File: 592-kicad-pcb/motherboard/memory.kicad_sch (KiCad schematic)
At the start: 13 parts, among them J15 Micro_SD_Card, J16 Conn_02x01, U12 W25Q32JVSS, U13 SN74LVC1G3157DBVR

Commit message: updates to routing
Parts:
- renumbered C29 to C31, C30 to C32, C31 to C33, C32 to C34, C33 to C35, J15 to J19, J16 to J20, R54 to R48, R55 to R49, R47 to R50, U12 to U13, U13 to U14
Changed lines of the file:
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@@
 		(dnp no)
 		(fields_autoplaced yes)
-		(property "Reference" "#PWR0141"
+		(property "Reference" "#PWR0143"
 			(at 46.99 52.07 0)
 			(effects
@@
 			(project "motherboard"
 				(path "/5b0c97ac-fa03-4db8-b41b-0eee32b6f55d/f049e4ad-bebe-4338-850a-2727de737ae9/2022d8e8-455b-4f4a-b4b4-f79e7486e2af"
-					(reference "#PWR0141")
+					(reference "#PWR0143")
 					(unit 1)
 				)
@@
 		(on_board yes)
 		(dnp no)
-		(property "Reference" "C33"
+		(property "Reference" "C35"
 			(at 201.93 81.2862 0)
 			(effects
@@
 			(project "motherboard"
 				(path "/5b0c97ac-fa03-4db8-b41b-0eee32b6f55d/f049e4ad-bebe-4338-850a-2727de737ae9/2022d8e8-455b-4f4a-b4b4-f79e7486e2af"
-					(reference "C33")
+					(reference "C35")
 					(unit 1)
 				)
@@
 		(on_board yes)
 		(dnp no)
-		(property "Reference" "C31"
+		(property "Reference" "C33"
 			(at 113.284 66.548 0)
 			(effects
@@
 			(project "motherboard"
 				(path "/5b0c97ac-fa03-4db8-b41b-0eee32b6f55d/f049e4ad-bebe-4338-850a-2727de737ae9/2022d8e8-455b-4f4a-b4b4-f79e7486e2af"
-					(reference "C31")
+					(reference "C33")
 					(unit 1)
 				)
@@
 		(on_board yes)
 		(dnp no)
-		(property "Reference" "#PWR0149"
+		(property "Reference" "#PWR0155"
 			(at 193.04 95.25 0)
 			(effects
@@
 			(project "motherboard"
 				(path "/5b0c97ac-fa03-4db8-b41b-0eee32b6f55d/f049e4ad-bebe-4338-850a-2727de737ae9/2022d8e8-455b-4f4a-b4b4-f79e7486e2af"
-					(reference "#PWR0149")
+					(reference "#PWR0155")
 					(unit 1)
 				)
@@
 		(dnp no)
 		(fields_autoplaced yes)
-		(property "Reference" "R47"
+		(property "Reference" "R50"
 			(at 195.58 62.2299 0)
 			(effects
@@
 			(project "motherboard"
 				(path "/5b0c97ac-fa03-4db8-b41b-0eee32b6f55d/f049e4ad-bebe-4338-850a-2727de737ae9/2022d8e8-455b-4f4a-b4b4-f79e7486e2af"
-					(reference "R47")
+					(reference "R50")
 					(unit 1)
 				)
@@
 		(on_board yes)
 		(dnp no)
-		(property "Reference" "C29"
+		(property "Reference" "C31"
 			(at 94.234 131.318 0)
 			(effects
@@
 			(project "motherboard"
 				(path "/5b0c97ac-fa03-4db8-b41b-0eee32b6f55d/f049e4ad-bebe-4338-850a-2727de737ae9/2022d8e8-455b-4f4a-b4b4-f79e7486e2af"
-					(reference "C29")
+					(reference "C31")
 					(unit 1)
 				)
@@
 		(dnp no)
 		(fields_autoplaced yes)
-		(property "Reference" "#PWR0144"
+		(property "Reference" "#PWR0150"
 			(at 119.38 60.96 0)
 			(effects
@@
 			(project "motherboard"
 				(path "/5b0c97ac-fa03-4db8-b41b-0eee32b6f55d/f049e4ad-bebe-4338-850a-2727de737ae9/2022d8e8-455b-4f4a-b4b4-f79e7486e2af"
-					(reference "#PWR0144")
+					(reference "#PWR0150")
 					(unit 1)
 				)
@@
 		(on_board yes)
 		(dnp no)
-		(property "Reference" "#PWR0140"
+		(property "Reference" "#PWR0146"
 			(at 67.31 152.4 0)
 			(effects
@@
 			(project "motherboard"
 				(path "/5b0c97ac-fa03-4db8-b41b-0eee32b6f55d/f049e4ad-bebe-4338-850a-2727de737ae9/2022d8e8-455b-4f4a-b4b4-f79e7486e2af"
-					(reference "#PWR0140")
+					(reference "#PWR0146")
 					(unit 1)
 				)
@@
 		(on_board yes)
 		(dnp no)
-		(property "Reference" "#PWR0145"
+		(property "Reference" "#PWR0151"
 			(at 119.38 78.74 0)
 			(effects
@@
 			(project "motherboard"
 				(path "/5b0c97ac-fa03-4db8-b41b-0eee32b6f55d/f049e4ad-bebe-4338-850a-2727de737ae9/2022d8e8-455b-4f4a-b4b4-f79e7486e2af"
-					(reference "#PWR0145")
+					(reference "#PWR0151")
 					(unit 1)
 				)
@@
 		(on_board yes)
 		(dnp no)
-		(property "Reference" "U13"
+		(property "Reference" "U14"
 			(at 163.576 57.15 0)
 			(effects
@@
 			(project "motherboard"
 				(path "/5b0c97ac-fa03-4db8-b41b-0eee32b6f55d/f049e4ad-bebe-4338-850a-2727de737ae9/2022d8e8-455b-4f4a-b4b4-f79e7486e2af"
-					(reference "U13")
+					(reference "U14")
 					(unit 1)
 				)
@@
 		(dnp no)
 		(fields_autoplaced yes)
-		(property "Reference" "U12"
+		(property "Reference" "U13"
 			(at 78.74 129.5399 0)
 			(effects
@@
 			(project "motherboard"
 				(path "/5b0c97ac-fa03-4db8-b41b-0eee32b6f55d/f049e4ad-bebe-4338-850a-2727de737ae9/2022d8e8-455b-4f4a-b4b4-f79e7486e2af"
-					(reference "U12")
+					(reference "U13")
 					(unit 1)
 				)
@@
 		(dnp no)
 		(fields_autoplaced yes)
-		(property "Reference" "J15"
+		(property "Reference" "J19"
 			(at 88.265 44.45 0)
 			(effects
@@
 			(project "motherboard"
 				(path "/5b0c97ac-fa03-4db8-b41b-0eee32b6f55d/f049e4ad-bebe-4338-850a-2727de737ae9/2022d8e8-455b-4f4a-b4b4-f79e7486e2af"
-					(reference "J15")
+					(reference "J19")
 					(unit 1)
 				)
@@
 		(dnp yes)
 		(fields_autoplaced yes)
-		(property "Reference" "J16"
+		(property "Reference" "J20"
 			(at 186.69 80.01 0)
 			(effects
@@
 			(project "motherboard"
 				(path "/5b0c97ac-fa03-4db8-b41b-0eee32b6f55d/f049e4ad-bebe-4338-850a-2727de737ae9/2022d8e8-455b-4f4a-b4b4-f79e7486e2af"
-					(reference "J16")
+					(reference "J20")
 					(unit 1)
 				)
@@
 		(on_board yes)
 		(dnp no)
-		(property "Reference" "C30"
+		(property "Reference" "C32"
 			(at 103.124 131.318 0)
 			(effects
@@
 			(project "motherboard"
 				(path "/5b0c97ac-fa03-4db8-b41b-0eee32b6f55d/f049e4ad-bebe-4338-850a-2727de737ae9/2022d8e8-455b-4f4a-b4b4-f79e7486e2af"
-					(reference "C30")
+					(reference "C32")
 					(unit 1)
 				)
@@
 		(on_board yes)
 		(dnp no)
-		(property "Reference" "#PWR0138"
+		(property "Reference" "#PWR0144"
 			(at 46.99 77.47 0)
 			(effects
@@
 			(project "motherboard"
 				(path "/5b0c97ac-fa03-4db8-b41b-0eee32b6f55d/f049e4ad-bebe-4338-850a-2727de737ae9/2022d8e8-455b-4f4a-b4b4-f79e7486e2af"
-					(reference "#PWR0138")
+					(reference "#PWR0144")
 					(unit 1)
 				)
@@
 		(on_board yes)
 		(dnp no)
-		(property "Reference" "R55"
+		(property "Reference" "R49"
 			(at 58.42 52.0699 0)
 			(effects
@@
 			(project "motherboard"
 				(path "/5b0c97ac-fa03-4db8-b41b-0eee32b6f55d/f049e4ad-bebe-4338-850a-2727de737ae9/2022d8e8-455b-4f4a-b4b4-f79e7486e2af"
-					(reference "R55")
+					(reference "R49")
 					(unit 1)
 				)
@@
 		(on_board yes)
 		(dnp no)
-		(property "Reference" "C32"
+		(property "Reference" "C34"
 			(at 122.174 66.548 0)
 			(effects
@@
 			(project "motherboard"
 				(path "/5b0c97ac-fa03-4db8-b41b-0eee32b6f55d/f049e4ad-bebe-4338-850a-2727de737ae9/2022d8e8-455b-4f4a-b4b4-f79e7486e2af"
-					(reference "C32")
+					(reference "C34")
 					(unit 1)
 				)
@@
 		(dnp no)
 		(fields_autoplaced yes)
-		(property "Reference" "#PWR0137"
+		(property "Reference" "#PWR0145"
 			(at 67.31 116.84 0)
 			(effects
@@
 			(project ""
 				(path "/5b0c97ac-fa03-4db8-b41b-0eee32b6f55d/f049e4ad-bebe-4338-850a-2727de737ae9/2022d8e8-455b-4f4a-b4b4-f79e7486e2af"
-					(reference "#PWR0137")
+					(reference "#PWR0145")
 					(unit 1)
 				)
@@
 		(dnp no)
 		(fields_autoplaced yes)
-		(property "Reference" "#PWR0139"
+		(property "Reference" "#PWR0147"
 			(at 100.33 125.73 0)
 			(effects
@@
 			(project "motherboard"
 				(path "/5b0c97ac-fa03-4db8-b41b-0eee32b6f55d/f049e4ad-bebe-4338-850a-2727de737ae9/2022d8e8-455b-4f4a-b4b4-f79e7486e2af"
-					(reference "#PWR0139")
+					(reference "#PWR0147")
 					(unit 1)
 				)
@@
 		(on_board yes)
 		(dnp no)
-		(property "Reference" "R54"
+		(property "Reference" "R48"
 			(at 53.34 116.8399 0)
 			(effects
@@
 			(project "motherboard"
 				(path "/5b0c97ac-fa03-4db8-b41b-0eee32b6f55d/f049e4ad-bebe-4338-850a-2727de737ae9/2022d8e8-455b-4f4a-b4b4-f79e7486e2af"
-					(reference "R54")
+					(reference "R48")
 					(unit 1)
 				)
@@
 		(dnp no)
 		(fields_autoplaced yes)
-		(property "Reference" "#PWR0148"
+		(property "Reference" "#PWR0154"
 			(at 193.04 60.96 0)
 			(effects
@@
 			(project "motherboard"
 				(path "/5b0c97ac-fa03-4db8-b41b-0eee32b6f55d/f049e4ad-bebe-4338-850a-2727de737ae9/2022d8e8-455b-4f4a-b4b4-f79e7486e2af"
-					(reference "#PWR0148")
+					(reference "#PWR0154")
 					(unit 1)
 				)
@@
 		(dnp no)
 		(fields_autoplaced yes)
-		(property "Reference" "#PWR0146"
+		(property "Reference" "#PWR0152"
 			(at 172.72 55.88 0)
 			(effects
@@
 			(project "motherboard"
 				(path "/5b0c97ac-fa03-4db8-b41b-0eee32b6f55d/f049e4ad-bebe-4338-850a-2727de737ae9/2022d8e8-455b-4f4a-b4b4-f79e7486e2af"
-					(reference "#PWR0146")
+					(reference "#PWR0152")
 					(unit 1)
 				)
@@
 		(on_board yes)
 		(dnp no)
-		(property "Reference" "#PWR0143"
+		(property "Reference" "#PWR0149"
 			(at 111.76 95.25 0)
 			(effects
@@
 			(project "motherboard"
 				(path "/5b0c97ac-fa03-4db8-b41b-0eee32b6f55d/f049e4ad-bebe-4338-850a-2727de737ae9/2022d8e8-455b-4f4a-b4b4-f79e7486e2af"
-					(reference "#PWR0143")
+					(reference "#PWR0149")
 					(unit 1)
 				)
@@
 		(on_board yes)
 		(dnp no)
-		(property "Reference" "#PWR0147"
+		(property "Reference" "#PWR0153"
 			(at 172.72 86.36 0)
 			(effects
@@
 			(project "motherboard"
 				(path "/5b0c97ac-fa03-4db8-b41b-0eee32b6f55d/f049e4ad-bebe-4338-850a-2727de737ae9/2022d8e8-455b-4f4a-b4b4-f79e7486e2af"
-					(reference "#PWR0147")
+					(reference "#PWR0153")
 					(unit 1)
 				)
@@
 		(on_board yes)
 		(dnp no)
-		(property "Reference" "#PWR0142"
+		(property "Reference" "#PWR0148"
 			(at 100.33 143.51 0)
 			(effects
@@
 			(project "motherboard"
 				(path "/5b0c97ac-fa03-4db8-b41b-0eee32b6f55d/f049e4ad-bebe-4338-850a-2727de737ae9/2022d8e8-455b-4f4a-b4b4-f79e7486e2af"
-					(reference "#PWR0142")
+					(reference "#PWR0148")
 					(unit 1)
 				)

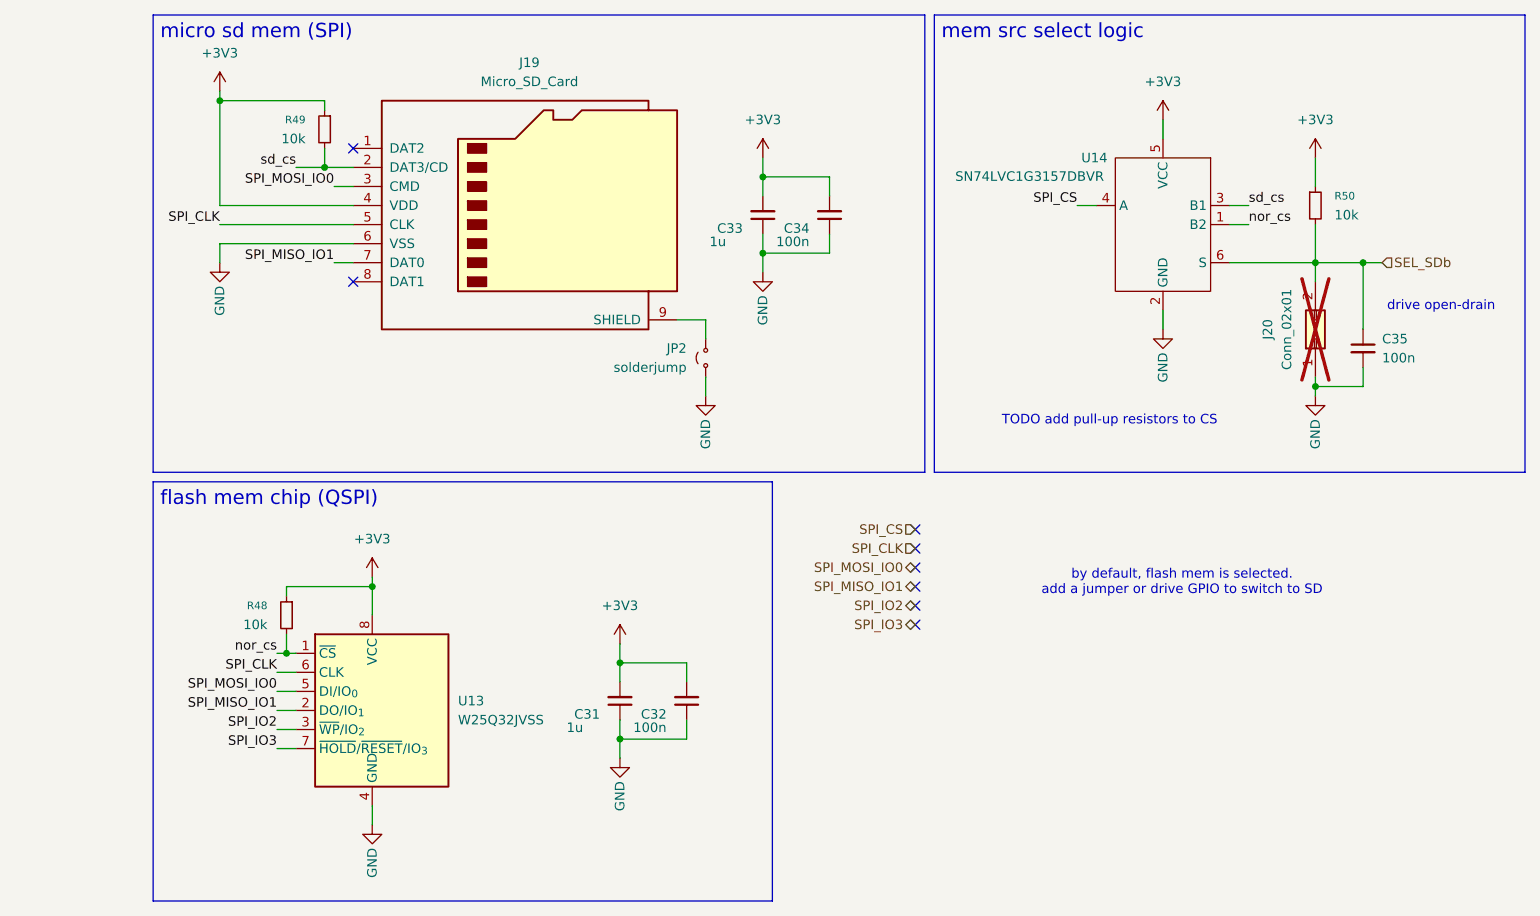
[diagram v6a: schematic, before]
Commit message: more routing progress, add termination resistors
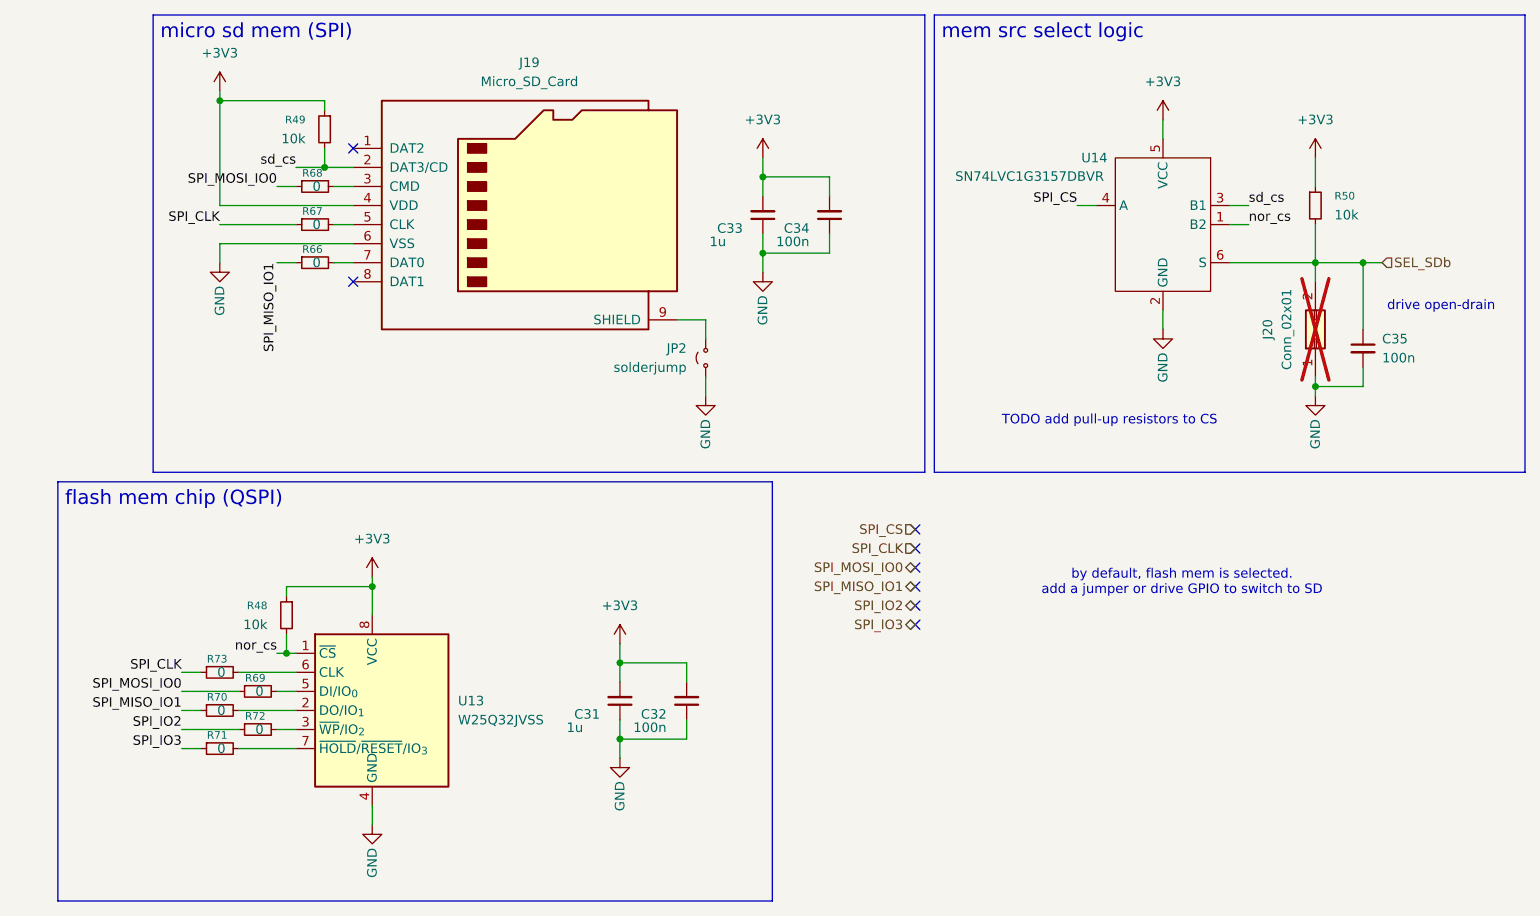
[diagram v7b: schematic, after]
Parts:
- added R66, R67, R68, R69, R70, R71, R72, R73: 0, Resistor_SMD:R_0402_1005Metric, symbol Device:R_Small
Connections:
- net SPI_CLK: now also R67.1, R73.1; no longer J19.5 (CLK), U13.6 (CLK)
- net SPI_IO2: now also R72.1; no longer U13.3 (~{WP}/IO_{2})
- net SPI_IO3: now also R71.1; no longer U13.7 (~{HOLD}/~{RESET}/IO_{3})
- net SPI_MISO_IO1: now also R66.1, R70.1; no longer J19.7 (DAT0), U13.2 (DO/IO_{1})
- net SPI_MOSI_IO0: now also R68.1, R69.1; no longer J19.3 (CMD), U13.5 (DI/IO_{0})
- new net: R71.2, U13.7 (~{HOLD}/~{RESET}/IO_{3})
- new net: J19.7 (DAT0), R66.2
- new net: R73.2, U13.6 (CLK)
- new net: R70.2, U13.2 (DO/IO_{1})
- new net: R72.2, U13.3 (~{WP}/IO_{2})
- new net: R69.2, U13.5 (DI/IO_{0})
- new net: J19.3 (CMD), R68.2
- new net: J19.5 (CLK), R67.2

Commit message: finalize termination
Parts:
- removed R68, R69, R70, R71, R72, R73: 0, Resistor_SMD:R_0402_1005Metric, symbol Device:R_Small
- R48, R49: value 10k -> 100k; footprint Resistor_SMD:R_0402_1005Metric -> (none); LCSC C25744 -> (none)
- R66: value 0 -> 27
- R67: value 0 -> 10k; LCSC (none) -> C25744
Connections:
- net +3V3: now also R67.1
- net SPI_CLK: now also J19.5 (CLK), U13.6 (CLK); no longer R67.1
- net SPI_IO2: now also U13.3 (~{WP}/IO_{2})
- net SPI_IO3: now also U13.7 (~{HOLD}/~{RESET}/IO_{3})
- net SPI_MISO_IO1: now also R67.2, U13.2 (DO/IO_{1})
- net SPI_MOSI_IO0: now also J19.3 (CMD), U13.5 (DI/IO_{0})
